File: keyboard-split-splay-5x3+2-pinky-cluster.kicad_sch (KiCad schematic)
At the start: 4 parts

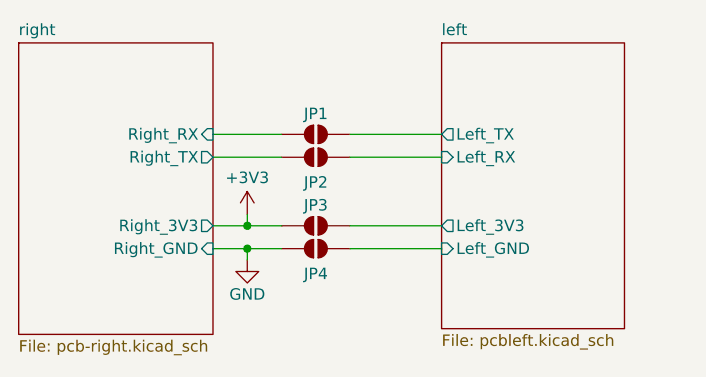
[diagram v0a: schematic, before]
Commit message: Rev 1.1, fix diode footprints, add plate and base generation jobs, add mouse bites and some extra solder jumpers
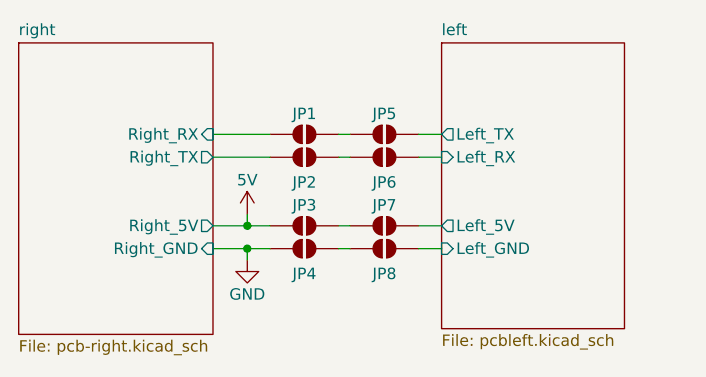
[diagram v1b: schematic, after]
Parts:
- added JP5, JP6, JP7, JP8: SolderJumper_2_Open, Jumper:SolderJumper-2_P1.3mm_Open_RoundedPad1.0x1.5mm, symbol Jumper:SolderJumper_2_Open
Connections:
- net left/Left_GND: now also JP8.2 (B); no longer JP4.2 (B)
- net left/Left_RX: now also JP6.2 (B); no longer JP2.2 (B)
- net left/Left_TX: now also JP5.2 (B); no longer JP1.2 (B)
- net +3V3 renamed 5V
- net left/Left_3V3: no longer names the net of JP3.2 (B)
- net left/Left_3V3: now also JP7.1 (A)
- new net: JP2.2 (B), JP6.1 (A)
- new net: JP1.2 (B), JP5.1 (A)
- new net: JP4.2 (B), JP8.1 (A)
- new net left/Left_5V: JP7.2 (B)
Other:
- sheet left ports: added Left_5V; removed Left_3V3
- sheet right ports: added Right_5V; removed Right_3V3
- moved on the sheet: JP1, JP2, JP3, JP4

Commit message: Latest release
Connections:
- net 5V: no longer JP3.1 (A)
- net GND: no longer JP4.1 (A)
- net left/Left_5V: no longer JP7.2 (B)
- net left/Left_GND: no longer JP8.2 (B)
- net left/Left_RX: no longer JP6.2 (B)
- net left/Left_TX: no longer JP5.2 (B)
- net right/Right_RX: no longer JP1.1 (A)
- net right/Right_TX: no longer JP2.1 (A)

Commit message: Through hole layout
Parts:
- removed JP1, JP2, JP3, JP4, JP5, JP6, JP7, JP8: SolderJumper_2_Open, Jumper:SolderJumper-2_P1.3mm_Open_RoundedPad1.0x1.5mm, symbol Jumper:SolderJumper_2_Open
- added J1, J2: (no value), benri-projects:JST_SM04B-SR_R, symbol benri-projects:CONNECTOR_JST_SM04B-SRSS-TB
- added J3, J4: Conn_01x04_Pin, symbol Connector:Conn_01x04_Pin
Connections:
- net left/Left_5V: now also J2.1
- net left/Left_GND: now also J2.4
- net left/Left_RX: now also J2.3
- net left/Left_TX: now also J2.2
- net right/Right_RX: now also J1.3
- net right/Right_TX: now also J1.2
- new net: J3.1 (Pin_1), J4.1 (Pin_1)
- new net: J3.2 (Pin_2), J4.2 (Pin_2)
- new net: J3.3 (Pin_3), J4.3 (Pin_3)
- new net: J3.4 (Pin_4), J4.4 (Pin_4)
- new net right/Right_5V: J1.4
- new net right/Right_GND: J1.1
